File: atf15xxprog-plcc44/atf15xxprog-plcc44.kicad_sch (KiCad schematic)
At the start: 8 parts, among them J1 AVR-JTAG-10, J2 Conn_01x19_Male, J3 Conn_01x19_Male, U1 atf15xx_PLCC44

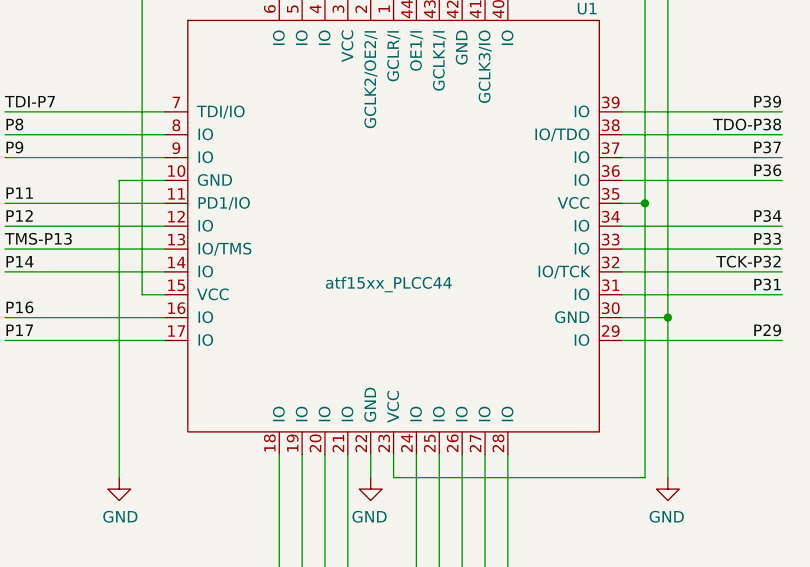
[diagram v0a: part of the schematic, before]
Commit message: atf15xxprog-plcc44: migrate sym lib to v6 format
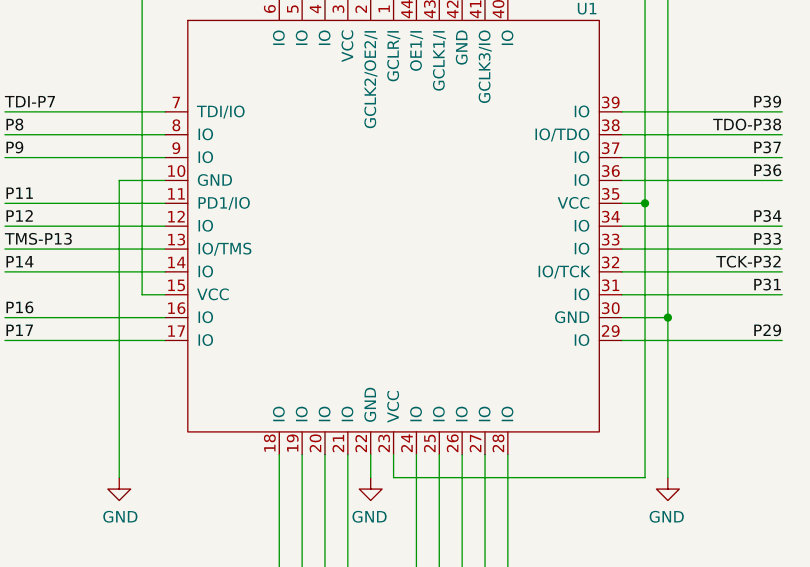
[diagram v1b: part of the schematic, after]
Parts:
- U1: value atf15xx_PLCC44 -> (none); footprint Package_LCC:PLCC-44_THT-Socket -> (none)
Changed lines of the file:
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@@
       (effects (font (size 1.27 1.27)) (justify left))
     )
-    (property "Value" "atf15xx_PLCC44" (id 1) (at 135.89 101.6 0)
+    (property "Value" "" (id 1) (at 135.89 101.6 0)
       (effects (font (size 1.27 1.27)) (justify left))
     )
-    (property "Footprint" "Package_LCC:PLCC-44_THT-Socket" (id 2) (at 143.51 95.25 0)
+    (property "Footprint" "" (id 2) (at 143.51 95.25 0)
       (effects (font (size 1.27 1.27)) hide)
     )

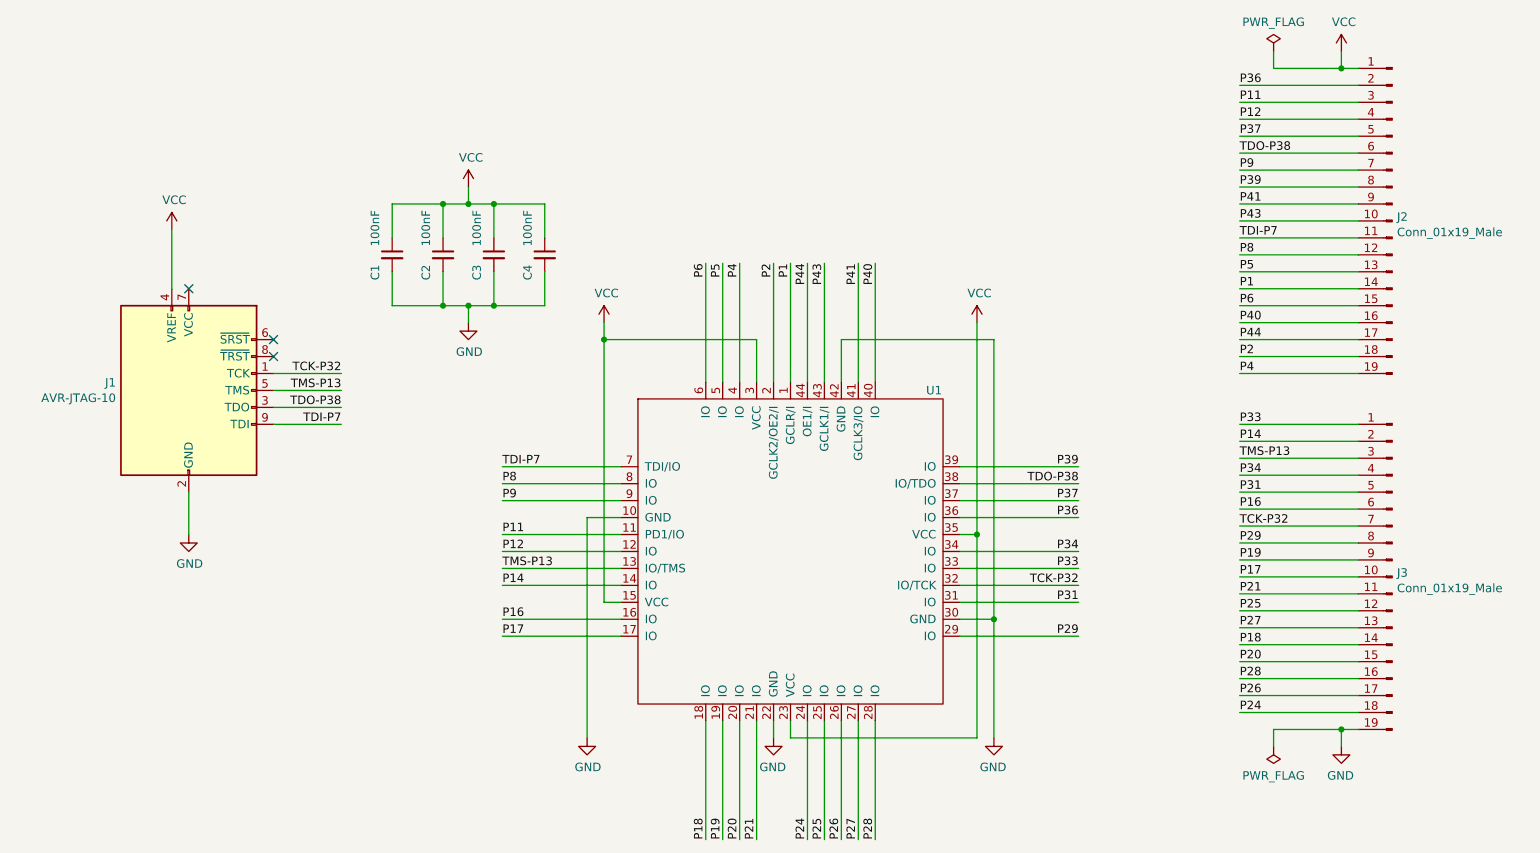
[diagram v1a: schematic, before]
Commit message: atf15xxprog-plcc44: use a custom JTAG-A symbol
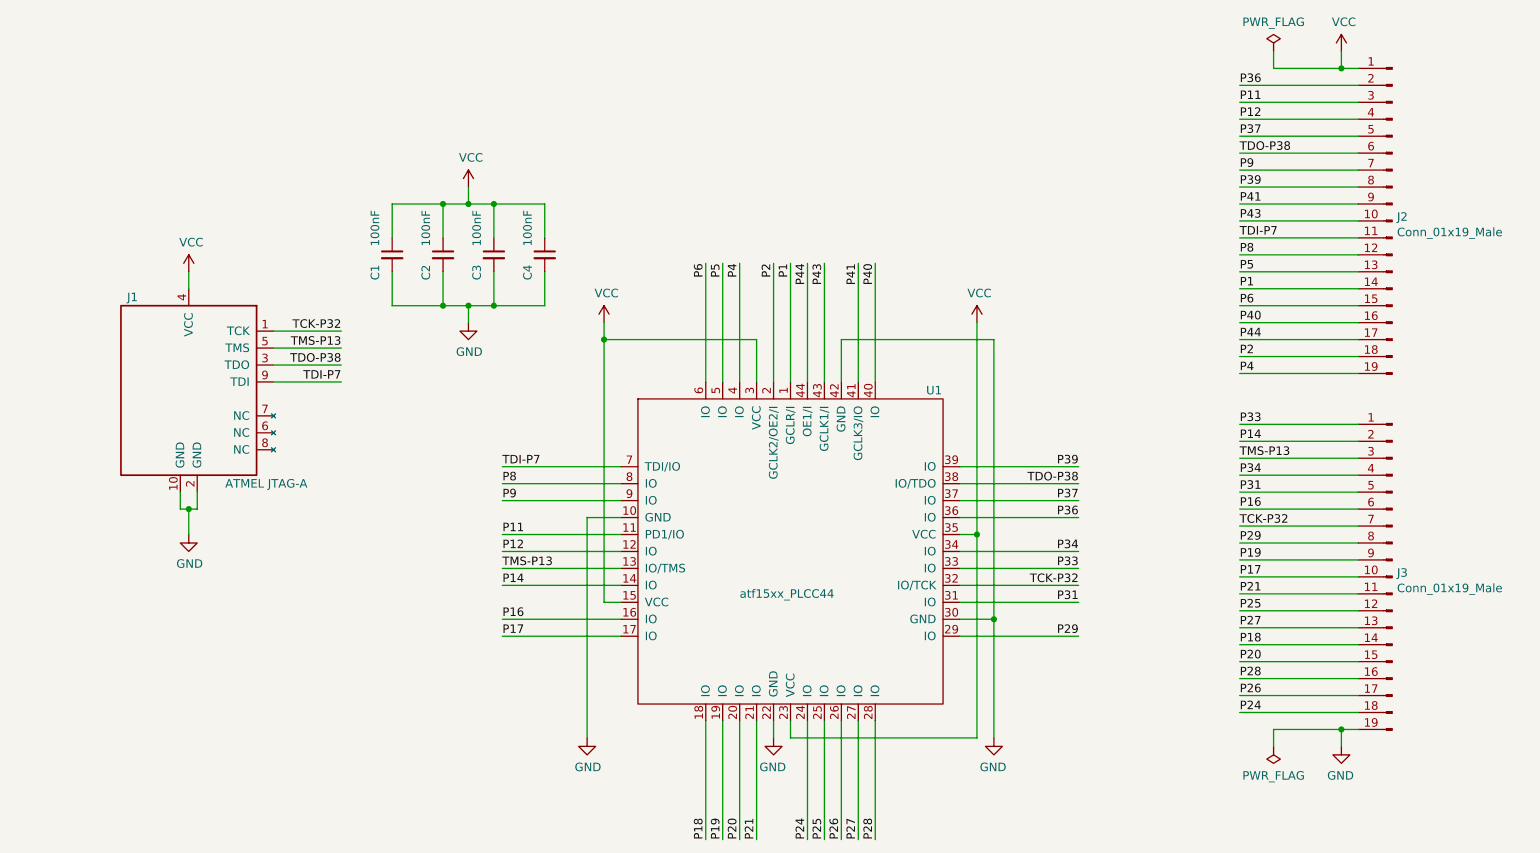
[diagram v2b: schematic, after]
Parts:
- J1: value AVR-JTAG-10 -> ATMEL JTAG-A; symbol Connector:AVR-JTAG-10 -> atf15xxprog:ATMEL JTAG-A
- U1: value (none) -> atf15xx_PLCC44; footprint (none) -> Package_LCC:PLCC-44_THT-Socket
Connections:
- no-connect marks 3 -> 0
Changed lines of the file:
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@@
   (junction (at 226.06 22.86) (diameter 0) (color 0 0 0 0)
   )
+  (junction (at 53.34 88.9) (diameter 0) (color 0 0 0 0)
+  )
   (junction (at 99.06 58.42) (diameter 0) (color 0 0 0 0)
   )
@@
   (junction (at 91.44 43.18) (diameter 0) (color 0 0 0 0)
   )
-  (no_connect (at 53.34 55.88))
-  (no_connect (at 66.04 66.04))
-  (no_connect (at 66.04 63.5))
   (wire (pts (xy 210.82 93.98) (xy 228.6 93.98))
     (stroke (width 0) (type default) (color 0 0 0 0))
@@
     (stroke (width 0) (type default) (color 0 0 0 0))
   )
+  (wire (pts (xy 52.07 88.9) (xy 52.07 86.36))
+    (stroke (width 0) (type default) (color 0 0 0 0))
+  )
   (wire (pts (xy 173.99 123.19) (xy 173.99 105.41))
     (stroke (width 0) (type default) (color 0 0 0 0))
@@
     (stroke (width 0) (type default) (color 0 0 0 0))
   )
-  (wire (pts (xy 66.04 71.12) (xy 76.2 71.12))
+  (wire (pts (xy 66.04 64.77) (xy 76.2 64.77))
     (stroke (width 0) (type default) (color 0 0 0 0))
   )
@@
     (stroke (width 0) (type default) (color 0 0 0 0))
   )
-  (wire (pts (xy 66.04 76.2) (xy 76.2 76.2))
+  (wire (pts (xy 66.04 69.85) (xy 76.2 69.85))
     (stroke (width 0) (type default) (color 0 0 0 0))
   )
@@
     (stroke (width 0) (type default) (color 0 0 0 0))
   )
-  (wire (pts (xy 50.8 46.99) (xy 50.8 55.88))
+  (wire (pts (xy 53.34 53.34) (xy 53.34 55.88))
     (stroke (width 0) (type default) (color 0 0 0 0))
   )
@@
     (stroke (width 0) (type default) (color 0 0 0 0))
   )
+  (wire (pts (xy 54.61 86.36) (xy 54.61 88.9))
+    (stroke (width 0) (type default) (color 0 0 0 0))
+  )
   (wire (pts (xy 228.6 25.4) (xy 210.82 25.4))
     (stroke (width 0) (type default) (color 0 0 0 0))
@@
     (stroke (width 0) (type default) (color 0 0 0 0))
   )
+  (wire (pts (xy 54.61 88.9) (xy 53.34 88.9))
+    (stroke (width 0) (type default) (color 0 0 0 0))
+  )
   (wire (pts (xy 228.6 40.64) (xy 210.82 40.64))
     (stroke (width 0) (type default) (color 0 0 0 0))
@@
     (stroke (width 0) (type default) (color 0 0 0 0))
   )
-  (wire (pts (xy 53.34 92.71) (xy 53.34 86.36))
-    (stroke (width 0) (type default) (color 0 0 0 0))
-  )
   (wire (pts (xy 228.6 111.76) (xy 210.82 111.76))
     (stroke (width 0) (type default) (color 0 0 0 0))
@@
     (stroke (width 0) (type default) (color 0 0 0 0))
   )
+  (wire (pts (xy 53.34 88.9) (xy 52.07 88.9))
+    (stroke (width 0) (type default) (color 0 0 0 0))
+  )
   (wire (pts (xy 210.82 60.96) (xy 228.6 60.96))
     (stroke (width 0) (type default) (color 0 0 0 0))
@@
     (stroke (width 0) (type default) (color 0 0 0 0))
   )
-  (wire (pts (xy 76.2 68.58) (xy 66.04 68.58))
+  (wire (pts (xy 76.2 62.23) (xy 66.04 62.23))
     (stroke (width 0) (type default) (color 0 0 0 0))
   )
@@
     (stroke (width 0) (type default) (color 0 0 0 0))
   )
+  (wire (pts (xy 53.34 92.71) (xy 53.34 88.9))
+    (stroke (width 0) (type default) (color 0 0 0 0))
+  )
   (wire (pts (xy 106.68 43.18) (xy 106.68 48.26))
     (stroke (width 0) (type default) (color 0 0 0 0))
@@
     (stroke (width 0) (type default) (color 0 0 0 0))
   )
-  (wire (pts (xy 76.2 73.66) (xy 66.04 73.66))
+  (wire (pts (xy 76.2 67.31) (xy 66.04 67.31))
     (stroke (width 0) (type default) (color 0 0 0 0))
   )
@@
     (effects (font (size 1.27 1.27)) (justify left bottom))
   )
-  (label "TDO-P38" (at 76.2 73.66 180)
+  (label "TDO-P38" (at 76.2 67.31 180)
     (effects (font (size 1.27 1.27)) (justify right bottom))
   )
@@
     (effects (font (size 1.27 1.27)) (justify left bottom))
   )
-  (label "TCK-P32" (at 76.2 68.58 180)
+  (label "TCK-P32" (at 76.2 62.23 180)
     (effects (font (size 1.27 1.27)) (justify right bottom))
   )
@@
     (effects (font (size 1.27 1.27)) (justify left bottom))
   )
-  (label "TDI-P7" (at 76.2 76.2 180)
+  (label "TDI-P7" (at 76.2 69.85 180)
     (effects (font (size 1.27 1.27)) (justify right bottom))
   )
@@
     (effects (font (size 1.27 1.27)) (justify left bottom))
   )
-  (label "TMS-P13" (at 76.2 71.12 180)
+  (label "TMS-P13" (at 76.2 64.77 180)
     (effects (font (size 1.27 1.27)) (justify right bottom))
   )
@@
       (effects (font (size 1.27 1.27)) (justify left))
     )
-    (property "Value" "" (id 1) (at 135.89 101.6 0)
+    (property "Value" "atf15xx_PLCC44" (id 1) (at 135.89 101.6 0)
       (effects (font (size 1.27 1.27)) (justify left))
     )
-    (property "Footprint" "" (id 2) (at 143.51 95.25 0)
+    (property "Footprint" "Package_LCC:PLCC-44_THT-Socket" (id 2) (at 143.51 95.25 0)
       (effects (font (size 1.27 1.27)) hide)
     )
@@
     (pin "9")
   )
-  (symbol (lib_id "Connector:AVR-JTAG-10") (at 53.34 71.12 0) (unit 1)
-    (in_bom yes) (on_board yes)
-    (property "Reference" "J1" (id 0) (at 42.418 69.9516 0)
+  (symbol (lib_id "atf15xxprog:ATMEL JTAG-A") (at 53.34 71.12 0) (unit 1)
+    (in_bom yes) (on_board yes)
+    (property "Reference" "J1" (id 0) (at 45.72 57.15 0)
       (effects (font (size 1.27 1.27)) (justify right))
     )
-    (property "Value" "AVR-JTAG-10" (id 1) (at 42.418 72.263 0)
+    (property "Value" "ATMEL JTAG-A" (id 1) (at 71.12 85.09 0)
       (effects (font (size 1.27 1.27)) (justify right))
     )
-    (property "Footprint" "Connector_IDC:IDC-Header_2x05_P2.54mm_Vertical" (id 2) (at 49.53 67.31 90)
+    (property "Footprint" "Connector_IDC:IDC-Header_2x05_P2.54mm_Vertical" (id 2) (at 19.05 66.04 90)
       (effects (font (size 1.27 1.27)) hide)
     )
@@
     (pin "1")
   )
-  (symbol (lib_id "power:VCC") (at 50.8 46.99 0) (unit 1)
-    (in_bom yes) (on_board yes)
-    (property "Reference" "#PWR01" (id 0) (at 50.8 50.8 0)
-      (effects (font (size 1.27 1.27)) hide)
-    )
-    (property "Value" "VCC" (id 1) (at 51.181 42.5958 0))
-    (property "Footprint" "" (id 2) (at 50.8 46.99 0)
-      (effects (font (size 1.27 1.27)) hide)
-    )
-    (property "Datasheet" "" (id 3) (at 50.8 46.99 0)
+  (symbol (lib_id "power:VCC") (at 53.34 53.34 0) (unit 1)
+    (in_bom yes) (on_board yes)
+    (property "Reference" "#PWR01" (id 0) (at 53.34 57.15 0)
+      (effects (font (size 1.27 1.27)) hide)
+    )
+    (property "Value" "VCC" (id 1) (at 53.721 48.9458 0))
+    (property "Footprint" "" (id 2) (at 53.34 53.34 0)
+      (effects (font (size 1.27 1.27)) hide)
+    )
+    (property "Datasheet" "" (id 3) (at 53.34 53.34 0)
       (effects (font (size 1.27 1.27)) hide)
     )
@@
     )
     (path "/00000000-0000-0000-0000-0000600e7666"
-      (reference "J1") (unit 1) (value "AVR-JTAG-10") (footprint "Connector_IDC:IDC-Header_2x05_P2.54mm_Vertical")
+      (reference "J1") (unit 1) (value "ATMEL JTAG-A") (footprint "Connector_IDC:IDC-Header_2x05_P2.54mm_Vertical")
     )
     (path "/00000000-0000-0000-0000-00006015d0fb"

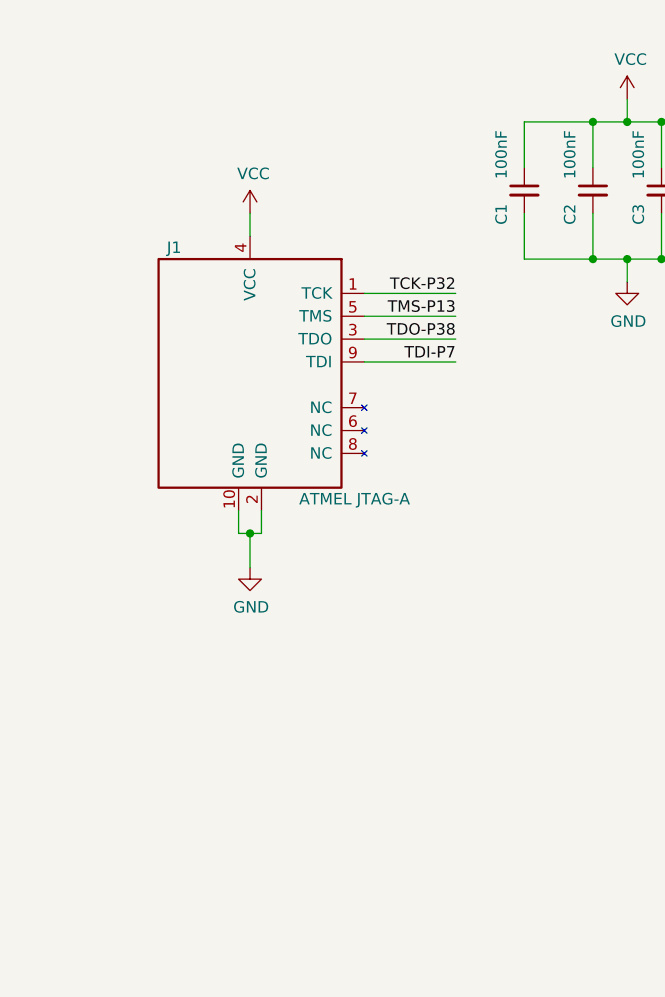
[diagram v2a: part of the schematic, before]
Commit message: atf15xxprog-plcc44: add pull-up resistors for JTAG
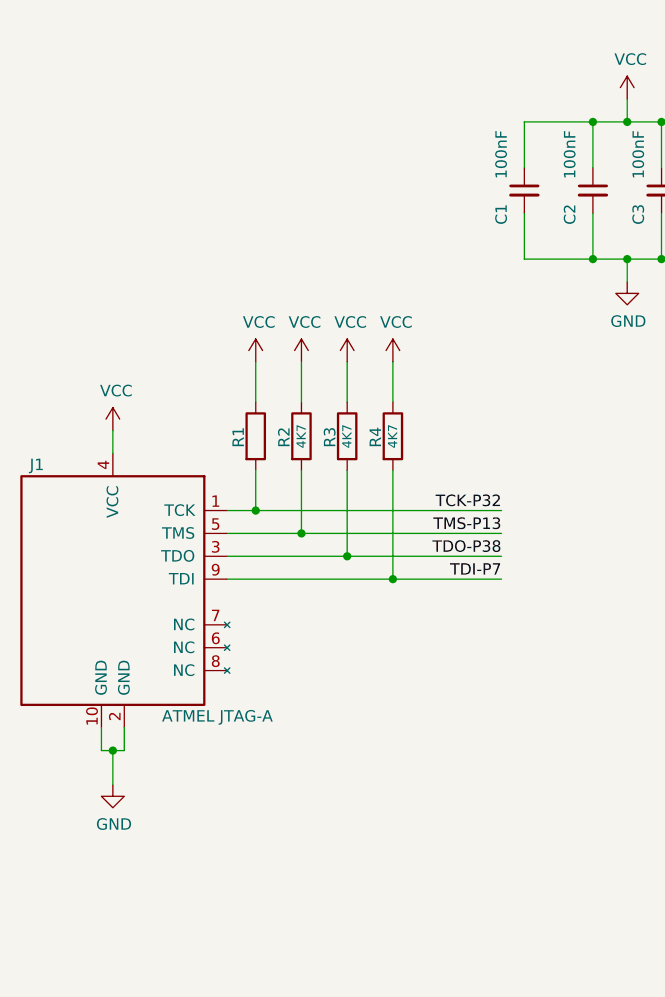
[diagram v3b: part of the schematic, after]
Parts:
- added R1: (no value), symbol Device:R
- added R2, R3, R4: 4K7, symbol Device:R
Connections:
- net TCK-P32: now also R1.2
- net TDI-P7: now also R4.2
- net TDO-P38: now also R3.2
- net TMS-P13: now also R2.2
- net VCC: now also R1.1, R2.1, R3.1, R4.1
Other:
- moved on the sheet: J1
